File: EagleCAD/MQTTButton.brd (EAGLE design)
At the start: 61 x 20 mm, 14 parts, among them SW2 SPST_TACT-EVQQ2

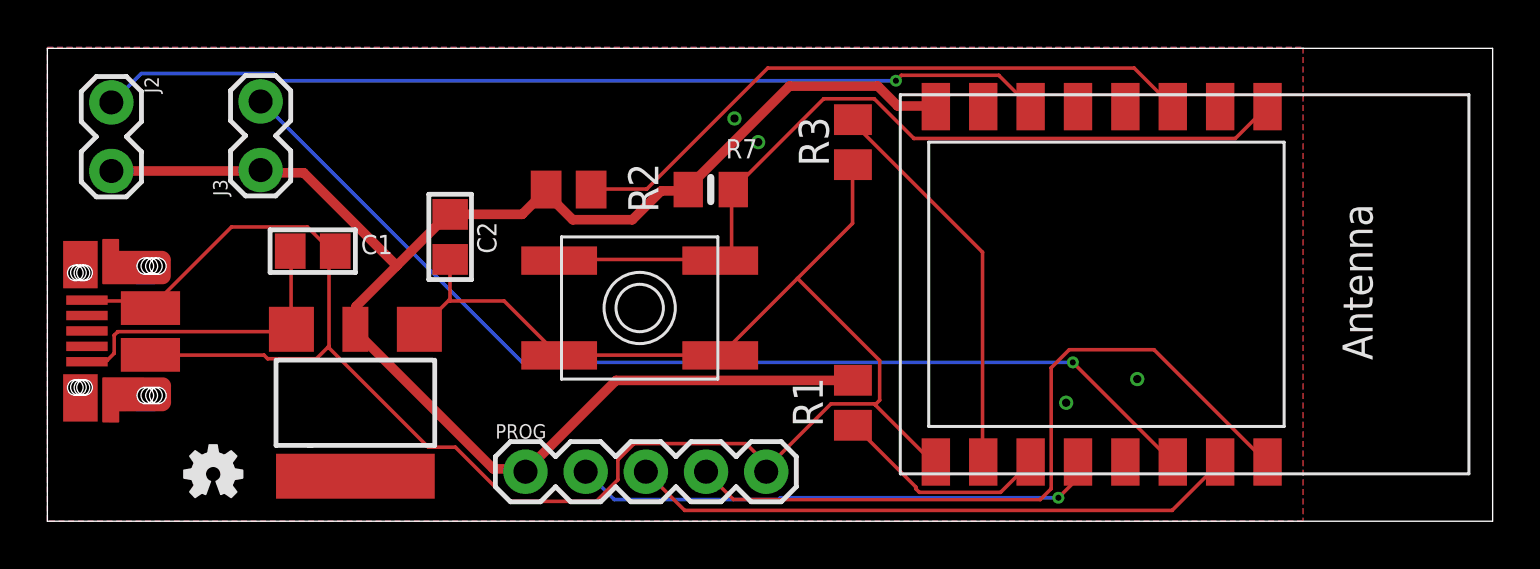
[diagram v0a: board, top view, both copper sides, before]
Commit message: updated design to include pull-down resistors on button input lines
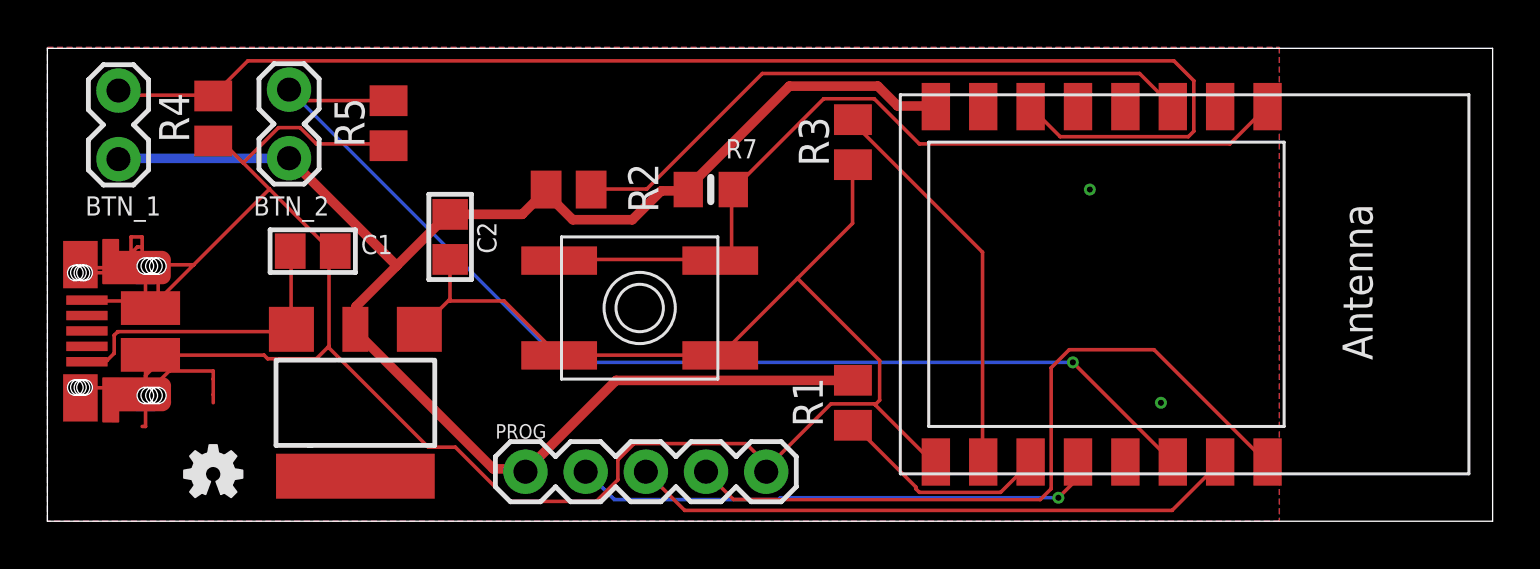
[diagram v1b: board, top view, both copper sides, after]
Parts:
- added R4, R5: 10k, adafruit:M0805
- moved J3 1.30 mm to (10.2, 15.5)
- moved J2 0.58 mm to (3.00, 18.0)
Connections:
- net BUTTON_1: now also R4.2
- net BUTTON_2: now also R5.2
- net GND: now also R4.1, R5.1
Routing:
- net GND: track 90.6 -> 130.8 mm, vias 4 -> 2
- net BUTTON_1: track 40.1 -> 56.1 mm, vias 1 -> 0
- net BUTTON_2: track 44.8 -> 48.2 mm
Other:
- board text added: "2/23/2019"
- board text added: "BTN_1"
- board text added: "BTN_2"
- board text added: "v1.2"
- board text removed: "2/12/2019"
- board text removed: "v1.0"

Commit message: fixed usb connector, rerouted
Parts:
- moved R3 7.00 mm to (34.0, 9.00)
- moved R7 3.16 mm to (31.0, 15.0), turned to 0 degrees
- moved R2 1.00 mm to (22.0, 15.0), turned to 270 degrees
- turned J1 to 270 degrees
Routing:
- net GND: track 130.8 -> 81.1 mm, vias 2 -> 8
- net BUTTON_1: track 56.1 -> 43.2 mm
- net RX: track 25.8 -> 34.7 mm
- net GPIO15: track 16.7 -> 9.74 mm
- net TX: track 31.8 -> 24.9 mm, vias 0 -> 1
- net +5V: track 13.0 -> 9.29 mm
- net BUTTON_2: track 48.2 -> 45.8 mm, vias 1 -> 0
- net 3.3V: track 69.6 -> 71.5 mm, vias 0 -> 2
- net RESET: track 35.7 -> 34.5 mm
- net GPIO0: track 22.3 -> 21.9 mm, vias 1 -> 0
